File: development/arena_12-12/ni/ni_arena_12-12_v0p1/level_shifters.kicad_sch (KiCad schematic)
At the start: 15 parts, among them U1 TXB0108PW, U2 TXB0108PW, U3 TXB0108PW, U4 TXB0108PW, U5 TXB0108PW

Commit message: Worked on schematic adding series termination resistors and buffers.
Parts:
- removed C1, C10, C2, C3, C4, C5, C6, C7, C8, C9: 0.1uF, Capacitor_SMD:C_0603_1608Metric, symbol Device:C
- removed U1, U5: TXB0108PW, Package_SO:TSSOP-20_4.4x6.5mm_P0.65mm, symbol TXB0108:TXB0108PW
- added C15, C16, C17, C18, C19, C20, C21, C22, C23, C24, C25, C26, C27: 0.1uF, symbol Device:C_Small
- added R100, R101, R102, R103, R104, R105, R106, R107, R108, R109, R110, R111, R112, R113, R114, R115, R116, R117, R118, R119, R120, R121, R122, R123, R124, R125, R126, R127, R128, R129, R130, R131, R132, R133, R134, R135, R136, R137, R138, R139, R140, R141, R142, R143, R144, R145, R146, R147, R148, R149, R150, R151, R152, R153, R154, R155, R156, R157, R158, R159, R160, R41, R42, R43, R44, R45, R46, R47, R48, R49, R50, R51, R52, R53, R54, R55, R56, R57, R58, R59, R60, R61, R62, R63, R64, R65, R66, R67, R68, R69, R70, R71, R72, R73, R74, R75, R76, R77, R78, R79, R80, R81, R82, R83, R84, R85, R86, R87, R88, R89, R90, R91, R92, R93, R94, R95, R96, R97, R98, R99: 33, symbol Device:R
- added U10, U11, U12, U14, U15, U16, U18, U21, U25, U6, U7, U8: TXB0108PW, symbol TXB0108:TXB0108PW
- added U13, U17, U19, U20, U22, U23, U24, U26, U27, U28, U29, U5, U9: 74LVC2G17, symbol 74xGxx:74LVC2G17
- U2, U3, U4: footprint Package_SO:TSSOP-20_4.4x6.5mm_P0.65mm -> (none)
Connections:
- net PAN3V.SCK_01 is gone; now on an unnamed net: U2.3 (A2)
- net PAN3V.SCK_02 is gone; now on an unnamed net: U2.4 (A3)
- net PAN3V.SCK_03 is gone; now on an unnamed net: U2.5 (A4)
- net PAN3V.SCK_04 is gone; now on an unnamed net: U2.6 (A5)
- net PAN3V.SCK_05 is gone; now on an unnamed net: U2.7 (A6)
- net +3.3V: now also C15.1, C16.1, C17.1, C18.1, C19.1, C20.1, C21.1, C22.1, C23.1, C24.1, C25.1, C26.1, C27.1, U10.10 (OE), U10.2 (VCCA), U11.10 (OE), U11.2 (VCCA), U12.10 (OE), U12.2 (VCCA), U13.5 (VCC), U14.10 (OE), U14.2 (VCCA), U15.10 (OE), U15.2 (VCCA), U16.10 (OE), U16.2 (VCCA), U17.5 (VCC), U18.10 (OE), U18.2 (VCCA), U19.5 (VCC), U20.5 (VCC), U21.10 (OE), U21.2 (VCCA), U22.5 (VCC), U23.5 (VCC), U24.5 (VCC), U25.10 (OE), U25.2 (VCCA), U26.5 (VCC), U27.5 (VCC), U28.5 (VCC), U29.5 (VCC), U5.5 (VCC), U6.10 (OE), U6.2 (VCCA), U7.10 (OE), U7.2 (VCCA), U8.10 (OE), U8.2 (VCCA), U9.5 (VCC)
- net +5V: now also U10.19 (VCCB), U11.19 (VCCB), U12.19 (VCCB), U14.19 (VCCB), U15.19 (VCCB), U16.19 (VCCB), U18.19 (VCCB), U21.19 (VCCB), U25.19 (VCCB), U6.19 (VCCB), U7.19 (VCCB), U8.19 (VCCB)
- net GND: now also C15.2, C16.2, C17.2, C18.2, C19.2, C20.2, C21.2, C22.2, C23.2, C24.2, C25.2, C26.2, C27.2, U10.11 (GND), U11.11 (GND), U12.11 (GND), U13.2 (GND), U14.11 (GND), U15.11 (GND), U16.11 (GND), U17.2 (GND), U18.11 (GND), U19.2 (GND), U20.2 (GND), U21.11 (GND), U22.2 (GND), U23.2 (GND), U24.2 (GND), U25.11 (GND), U26.2 (GND), U27.2 (GND), U28.2 (GND), U29.2 (GND), U5.2 (GND), U6.11 (GND), U7.11 (GND), U8.11 (GND), U9.2 (GND)
- net PAN3V.MISO_00: now also U23.3; no longer U2.9 (A8)
- net PAN3V.MISO_01: now also U24.3; no longer U3.3 (A2)
- net PAN3V.MISO_02: now also U26.3; no longer U3.5 (A4)
- net PAN3V.MISO_03: now also U27.3; no longer U3.7 (A6)
- net PAN3V.MISO_04: now also U28.3; no longer U3.9 (A8)
- net PAN3V.MISO_05: now also U29.3; no longer U4.3 (A2)
- net PAN3V.MISO_06: no longer U4.5 (A4)
- net PAN3V.MISO_07: no longer U4.7 (A6)
- net PAN3V.MISO_08: no longer U4.9 (A8)
- net PAN3V.MOSI_00: now also U23.1; no longer U2.8 (A7)
- net PAN3V.MOSI_01: now also U24.1; no longer U3.1 (A1)
- net PAN3V.MOSI_02: now also U26.1; no longer U3.4 (A3)
- net PAN3V.MOSI_03: now also U27.1; no longer U3.6 (A5)
- net PAN3V.MOSI_04: now also U28.1; no longer U3.8 (A7)
- net PAN3V.MOSI_05: now also U29.1; no longer U4.1 (A1)
- net PAN3V.MOSI_06: no longer U4.4 (A3)
- net PAN3V.MOSI_07: no longer U4.6 (A5)
- net PAN3V.MOSI_08: no longer U4.8 (A7)
- net PAN5V.MISO_00: now also R150.1; no longer U2.12 (B8)
- net PAN5V.MISO_01: now also R152.1; no longer U3.18 (B2)
- net PAN5V.MISO_02: now also R154.1; no longer U3.16 (B4)
- net PAN5V.MISO_03: now also R156.1; no longer U3.14 (B6)
- net PAN5V.MISO_04: now also R158.1; no longer U3.12 (B8)
- net PAN5V.MISO_05: now also R160.1; no longer U4.18 (B2)
- net PAN5V.MISO_06: no longer U4.16 (B4)
- net PAN5V.MISO_07: no longer U4.14 (B6)
- net PAN5V.MISO_08: no longer U4.12 (B8)
- net PAN5V.MOSI_00: now also R149.1; no longer U2.13 (B7)
- net PAN5V.MOSI_01: now also R151.1; no longer U3.20 (B1)
- net PAN5V.MOSI_02: now also R153.1; no longer U3.17 (B3)
- net PAN5V.MOSI_03: now also R155.1; no longer U3.15 (B5)
- net PAN5V.MOSI_04: now also R157.1; no longer U3.13 (B7)
- net PAN5V.MOSI_05: now also R159.1; no longer U4.20 (B1)
- net PAN5V.MOSI_06: no longer U4.17 (B3)
- net PAN5V.MOSI_07: no longer U4.15 (B5)
- net PAN5V.MOSI_08: no longer U4.13 (B7)
- net PAN5V.SCK_00: no longer U2.20 (B1)
- net PAN5V.SCK_01: no longer U2.18 (B2)
- net PAN5V.SCK_02: no longer U2.17 (B3)
- net PAN5V.SCK_03: no longer U2.16 (B4)
- net PAN5V.SCK_04: no longer U2.15 (B5)
- net PAN5V.SCK_05: no longer U2.14 (B6)
- net PAN3V.SCK_00: no longer names the net of U2.1 (A1)
- net PAN3V.SCK_00: now also U2.8 (A7), U2.9 (A8), U3.1 (A1), U3.3 (A2), U3.4 (A3), U3.5 (A4), U5.6
- new net: U21.6 (A5), U23.6
- new net: U11.6 (A5), U11.7 (A6), U11.8 (A7), U11.9 (A8), U12.1 (A1), U12.3 (A2), U12.4 (A3), U12.5 (A4), U12.6 (A5), U12.7 (A6), U12.8 (A7), U12.9 (A8), U13.4
- new net: R112.2, U12.12 (B8)
- new net: R111.2, U12.13 (B7)
- new net: R110.2, U12.14 (B6)
- new net: R109.2, U12.15 (B5)
- new net: R108.2, U12.16 (B4)
- new net: R107.2, U12.17 (B3)
- new net: R106.2, U12.18 (B2)
- new net: R105.2, U12.20 (B1)
- new net: R128.2, U15.12 (B8)
- new net: R50.2, U3.18 (B2)
- new net: R103.2, U11.13 (B7)
- new net: R153.2, U25.20 (B1)
- new net: R82.2, U8.18 (B2)
- new net: U6.1 (A1), U6.3 (A2), U6.4 (A3), U6.5 (A4), U6.6 (A5), U6.7 (A6), U6.8 (A7), U6.9 (A8), U7.1 (A1), U7.3 (A2), U7.4 (A3), U7.5 (A4), U9.6
- new net: R80.2, U7.12 (B8)
- new net: R79.2, U7.13 (B7)
- new net: R78.2, U7.14 (B6)
- new net: R77.2, U7.15 (B5)
- new net: R76.2, U7.16 (B4)
- new net: R75.2, U7.17 (B3)
- new net: R74.2, U7.18 (B2)
- new net: R73.2, U7.20 (B1)
- new net: U7.6 (A5), U7.7 (A6), U7.8 (A7), U7.9 (A8), U8.1 (A1), U8.3 (A2), U8.4 (A3), U8.5 (A4), U8.6 (A5), U8.7 (A6), U8.8 (A7), U8.9 (A8), U9.4
- new net: R142.2, U18.14 (B6)
- new net: R113.2, U14.20 (B1)
- new net: R120.2, U14.12 (B8)
- new net: R145.2, U21.20 (B1)
- new net: R86.2, U8.14 (B6)
- new net: R49.2, U3.20 (B1)
- new net: R127.2, U15.13 (B7)
- new net: R62.2, U4.14 (B6)
- new net: R150.2, U21.14 (B6)
- new net: R56.2, U3.12 (B8)
- new net: R55.2, U3.13 (B7)
- new net: R54.2, U3.14 (B6)
- new net: R53.2, U3.15 (B5)
- new net: R52.2, U3.16 (B4)
- new net: R51.2, U3.17 (B3)
- new net: U3.6 (A5), U3.7 (A6), U3.8 (A7), U3.9 (A8), U4.1 (A1), U4.3 (A2), U4.4 (A3), U4.5 (A4), U4.6 (A5), U4.7 (A6), U4.8 (A7), U4.9 (A8), U5.4
- new net: U15.6 (A5), U15.7 (A6), U15.8 (A7), U15.9 (A8), U16.1 (A1), U16.3 (A2), U16.4 (A3), U16.5 (A4), U16.6 (A5), U16.7 (A6), U16.8 (A7), U16.9 (A8), U17.4
- new net: R136.2, U16.12 (B8)
- new net: R135.2, U16.13 (B7)
- new net: R134.2, U16.14 (B6)
- new net: R133.2, U16.15 (B5)
- new net: R132.2, U16.16 (B4)
- new net: R131.2, U16.17 (B3)
- new net: R130.2, U16.18 (B2)
- new net: R129.2, U16.20 (B1)
- new net: U18.4 (A3), U18.5 (A4), U19.4
- new net: U14.1 (A1), U14.3 (A2), U14.4 (A3), U14.5 (A4), U14.6 (A5), U14.7 (A6), U14.8 (A7), U14.9 (A8), U15.1 (A1), U15.3 (A2), U15.4 (A3), U15.5 (A4), U17.6
- new net: R126.2, U15.14 (B6)
- new net: R125.2, U15.15 (B5)
- new net: R124.2, U15.16 (B4)
- new net: R123.2, U15.17 (B3)
- new net: R122.2, U15.18 (B2)
- new net: R121.2, U15.20 (B1)
- new net: R160.2, U25.12 (B8)
- new net: U18.1 (A1), U18.3 (A2), U19.6
- new net: R154.2, U25.18 (B2)
- new net: R157.2, U25.15 (B5)
- new net: R69.2, U6.15 (B5)
- new net: R59.2, U4.17 (B3)
- new net: R88.2, U8.12 (B8)
- new net: R84.2, U8.16 (B4)
- new net: U18.6 (A5), U18.7 (A6), U20.6
- new net: U10.1 (A1), U10.3 (A2), U10.4 (A3), U10.5 (A4), U10.6 (A5), U10.7 (A6), U10.8 (A7), U10.9 (A8), U11.1 (A1), U11.3 (A2), U11.4 (A3), U11.5 (A4), U13.6
- new net: R87.2, U8.13 (B7)
- new net: R118.2, U14.14 (B6)
- new net: U25.3 (A2), U26.4
- new net: R68.2, U6.16 (B4)
- new net: R46.2, U2.14 (B6)
- new net: U25.1 (A1), U26.6
- new net: R144.2, U18.12 (B8)
- new net: R143.2, U18.13 (B7)
- new net: R141.2, U18.15 (B5)
- new net: R140.2, U18.16 (B4)
- new net: R139.2, U18.17 (B3)
- new net: R138.2, U18.18 (B2)
- new net: R137.2, U18.20 (B1)
- new net: U18.8 (A7), U18.9 (A8), U20.4
- new net: R85.2, U8.15 (B5)
- new net: R83.2, U8.17 (B3)
- new net: R81.2, U8.20 (B1)
- new net: R66.2, U6.18 (B2)
- new net: R147.2, U21.17 (B3)
- new net: R43.2, U2.17 (B3)
- new net: R89.2, U10.20 (B1)
- new net: R149.2, U21.15 (B5)
- new net: R91.2, U10.17 (B3)
- new net: U25.8 (A7), U29.6
- new net: R63.2, U4.13 (B7)
- new net: R104.2, U11.12 (B8)
- new net: R102.2, U11.14 (B6)
- new net: R101.2, U11.15 (B5)
- new net: R100.2, U11.16 (B4)
- new net: R99.2, U11.17 (B3)
- new net: R98.2, U11.18 (B2)
- new net: R97.2, U11.20 (B1)
- new net: R116.2, U14.16 (B4)
- new net: R72.2, U6.12 (B8)
- new net: R115.2, U14.17 (B3)
- new net: R146.2, U21.18 (B2)
- new net: U21.1 (A1), U21.3 (A2), U22.6
- new net: R156.2, U25.16 (B4)
- new net: U21.9 (A8), U24.4
- new net: R151.2, U21.13 (B7)
- new net: R159.2, U25.13 (B7)
- new net: R158.2, U25.14 (B6)
- new net: R155.2, U25.17 (B3)
- new net: U25.4 (A3), U27.6
- new net: U25.5 (A4), U27.4
- new net: U25.6 (A5), U28.6
- new net: U25.7 (A6), U28.4
- new net: U25.9 (A8), U29.4
- new net: R117.2, U14.15 (B5)
- new net: R119.2, U14.13 (B7)
- new net: R114.2, U14.18 (B2)
- new net: U21.7 (A6), U23.4
- new net: R70.2, U6.14 (B6)
- new net: R60.2, U4.16 (B4)
- new net: R96.2, U10.12 (B8)
- new net: R95.2, U10.13 (B7)
- new net: R94.2, U10.14 (B6)
- new net: R93.2, U10.15 (B5)
- new net: R92.2, U10.16 (B4)
- new net: R90.2, U10.18 (B2)
- new net: R152.2, U21.12 (B8)
- new net: U21.8 (A7), U24.6
- new net: R48.2, U2.12 (B8)
- new net: R71.2, U6.13 (B7)
- new net: R58.2, U4.18 (B2)
- new net: R67.2, U6.17 (B3)
- new net: R41.2, U2.20 (B1)
- new net: U21.4 (A3), U21.5 (A4), U22.4
- new net: R44.2, U2.16 (B4)
- new net: R64.2, U4.12 (B8)
- new net: R61.2, U4.15 (B5)
- new net: R57.2, U4.20 (B1)
- new net: R42.2, U2.18 (B2)
- new net: R148.2, U21.16 (B4)
- new net: R65.2, U6.20 (B1)
- new net: R45.2, U2.15 (B5)
- new net: R47.2, U2.13 (B7)
- new net PAN3V.CS_0: U5.1
- new net PAN3V.CS_1: U5.3
- new net PAN3V.CS_2: U9.1
- new net PAN3V.CS_3: U9.3
- new net PAN3V.CS_4: U13.1
- new net PAN3V.CS_5: U13.3
- new net PAN3V.CS_6: U17.1
- new net PAN3V.CS_7: U17.3
- new net PAN3V.SCK_0: U19.1
- new net PAN3V.SCK_1: U19.3
- new net PAN3V.SCK_2: U20.1
- new net PAN3V.SCK_3: U20.3
- new net PAN3V.SCK_4: U22.1
- new net PAN3V.SCK_5: U22.3
- new net PAN5V.CS_0_P01: R41.1
- new net PAN5V.CS_0_P02: R42.1
- new net PAN5V.CS_0_P03: R43.1
- new net PAN5V.CS_0_P04: R44.1
- new net PAN5V.CS_0_P05: R45.1
- new net PAN5V.CS_0_P06: R46.1
- new net PAN5V.CS_0_P07: R47.1
- new net PAN5V.CS_0_P08: R48.1
- new net PAN5V.CS_0_P09: R49.1
- new net PAN5V.CS_0_P10: R50.1
- new net PAN5V.CS_0_P11: R51.1
- new net PAN5V.CS_0_P12: R52.1
- new net PAN5V.CS_1_P01: R53.1
- new net PAN5V.CS_1_P02: R54.1
- new net PAN5V.CS_1_P03: R55.1
- new net PAN5V.CS_1_P04: R56.1
- new net PAN5V.CS_1_P05: R57.1
- new net PAN5V.CS_1_P06: R58.1
- new net PAN5V.CS_1_P07: R59.1
- new net PAN5V.CS_1_P08: R60.1
- new net PAN5V.CS_1_P09: R61.1
- new net PAN5V.CS_1_P10: R62.1
- new net PAN5V.CS_1_P11: R63.1
- new net PAN5V.CS_1_P12: R64.1
- new net PAN5V.CS_2_P01: R65.1
- new net PAN5V.CS_2_P02: R66.1
- new net PAN5V.CS_2_P03: R67.1
- new net PAN5V.CS_2_P04: R68.1
- new net PAN5V.CS_2_P05: R69.1
- new net PAN5V.CS_2_P06: R70.1
- new net PAN5V.CS_2_P07: R71.1
- new net PAN5V.CS_2_P08: R72.1
- new net PAN5V.CS_2_P09: R73.1
- new net PAN5V.CS_2_P10: R74.1
- new net PAN5V.CS_2_P11: R75.1
- new net PAN5V.CS_2_P12: R76.1
- new net PAN5V.CS_3_P01: R77.1
- new net PAN5V.CS_3_P02: R78.1
- new net PAN5V.CS_3_P03: R79.1
- new net PAN5V.CS_3_P04: R80.1
- new net PAN5V.CS_3_P05: R81.1
- new net PAN5V.CS_3_P06: R82.1
- new net PAN5V.CS_3_P07: R83.1
- new net PAN5V.CS_3_P08: R84.1
- new net PAN5V.CS_3_P09: R85.1
- new net PAN5V.CS_3_P10: R86.1
- new net PAN5V.CS_3_P11: R87.1
- new net PAN5V.CS_3_P12: R88.1
- new net PAN5V.CS_4_P01: R89.1
- new net PAN5V.CS_4_P02: R90.1
- new net PAN5V.CS_4_P03: R91.1
- new net PAN5V.CS_4_P04: R92.1
- new net PAN5V.CS_4_P05: R93.1
- new net PAN5V.CS_4_P06: R94.1
- new net PAN5V.CS_4_P07: R95.1
- new net PAN5V.CS_4_P08: R96.1
- new net PAN5V.CS_4_P09: R97.1
- new net PAN5V.CS_4_P10: R98.1
- new net PAN5V.CS_4_P11: R99.1
- new net PAN5V.CS_4_P12: R100.1
- new net PAN5V.CS_5_P01: R101.1
- new net PAN5V.CS_5_P02: R102.1
- new net PAN5V.CS_5_P03: R103.1
- new net PAN5V.CS_5_P04: R104.1
- new net PAN5V.CS_5_P05: R105.1
- new net PAN5V.CS_5_P06: R106.1
- new net PAN5V.CS_5_P07: R107.1
- new net PAN5V.CS_5_P08: R108.1
- new net PAN5V.CS_5_P09: R109.1
- new net PAN5V.CS_5_P10: R110.1
- new net PAN5V.CS_5_P11: R111.1
- new net PAN5V.CS_5_P12: R112.1
- new net PAN5V.CS_6_P01: R113.1
- new net PAN5V.CS_6_P02: R114.1
- new net PAN5V.CS_6_P03: R115.1
- new net PAN5V.CS_6_P04: R116.1
- new net PAN5V.CS_6_P05: R117.1
- new net PAN5V.CS_6_P06: R118.1
- new net PAN5V.CS_6_P07: R119.1
- new net PAN5V.CS_6_P08: R120.1
- new net PAN5V.CS_6_P09: R121.1
- new net PAN5V.CS_6_P10: R122.1
- new net PAN5V.CS_6_P11: R123.1
- new net PAN5V.CS_6_P12: R124.1
- new net PAN5V.CS_7_P01: R125.1
- new net PAN5V.CS_7_P02: R126.1
- new net PAN5V.CS_7_P03: R127.1
- new net PAN5V.CS_7_P04: R128.1
- new net PAN5V.CS_7_P05: R129.1
- new net PAN5V.CS_7_P06: R130.1
- new net PAN5V.CS_7_P07: R131.1
- new net PAN5V.CS_7_P08: R132.1
- new net PAN5V.CS_7_P09: R133.1
- new net PAN5V.CS_7_P10: R134.1
- new net PAN5V.CS_7_P11: R135.1
- new net PAN5V.CS_7_P12: R136.1
- new net PAN5V.SCK_0_H1: R137.1
- new net PAN5V.SCK_0_H2: R138.1
- new net PAN5V.SCK_1_H1: R139.1
- new net PAN5V.SCK_1_H2: R140.1
- new net PAN5V.SCK_2_H1: R141.1
- new net PAN5V.SCK_2_H2: R142.1
- new net PAN5V.SCK_3_H1: R143.1
- new net PAN5V.SCK_3_H2: R144.1
- new net PAN5V.SCK_4_H1: R145.1
- new net PAN5V.SCK_4_H2: R146.1
- new net PAN5V.SCK_5_H1: R147.1
- new net PAN5V.SCK_5_H2: R148.1

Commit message: More work on schematic adding resistos and buffers.
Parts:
- added C28, C29, C30, C31: 0.1uF, symbol Device:C_Small
- added R161, R162, R163, R164, R165, R166, R167, R168: 33, symbol Device:R
- added U30: TXB0108PW, symbol TXB0108:TXB0108PW
- added U31, U32, U33, U34: 74LVC2G17, symbol 74xGxx:74LVC2G17
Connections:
- net PAN3V.MISO_00 is gone; now on net PAN5V.MISO_00: U23.3
- net PAN3V.MISO_01 is gone; now on net PAN5V.MISO_01: U24.3
- net PAN3V.MISO_02 is gone; now on net PAN5V.MISO_02: U26.3
- net PAN3V.MISO_03 is gone; now on net PAN5V.MISO_03: U27.3
- net PAN3V.MISO_04 is gone; now on net PAN5V.MISO_04: U28.3
- net PAN3V.MISO_05 is gone; now on net PAN5V.MISO_05: U29.3
- net PAN3V.MOSI_00 is gone; now on net PAN5V.MOSI_00: U23.1
- net PAN3V.MOSI_01 is gone; now on net PAN5V.MOSI_01: U24.1
- net PAN3V.MOSI_02 is gone; now on net PAN5V.MOSI_02: U26.1
- net PAN3V.MOSI_03 is gone; now on net PAN5V.MOSI_03: U27.1
- net PAN3V.MOSI_04 is gone; now on net PAN5V.MOSI_04: U28.1
- net PAN3V.MOSI_05 is gone; now on net PAN5V.MOSI_05: U29.1
- net +3.3V: now also C28.1, C29.1, C30.1, C31.1, U30.10 (OE), U30.2 (VCCA), U31.5 (VCC), U32.5 (VCC), U33.5 (VCC), U34.5 (VCC)
- net +5V: now also U30.19 (VCCB)
- net GND: now also C28.2, C29.2, C30.2, C31.2, U30.11 (GND), U31.2 (GND), U32.2 (GND), U33.2 (GND), U34.2 (GND)
- net PAN5V.MISO_06: now also R162.1, U31.3
- net PAN5V.MISO_07: now also R164.1, U33.3
- net PAN5V.MISO_08: now also R166.1, U32.3
- net PAN5V.MISO_09: now also R168.1, U34.3
- net PAN5V.MOSI_06: now also R161.1, U31.1
- net PAN5V.MOSI_07: now also R163.1, U33.1
- net PAN5V.MOSI_08: now also R165.1, U32.1
- net PAN5V.MOSI_09: now also R167.1, U34.1
- net PAN3V.CS_0 renamed PAN5V.CS_0
- net PAN3V.CS_1 renamed PAN5V.CS_1
- net PAN3V.CS_2 renamed PAN5V.CS_2
- net PAN3V.CS_3 renamed PAN5V.CS_3
- net PAN3V.CS_4 renamed PAN5V.CS_4
- net PAN3V.CS_5 renamed PAN5V.CS_5
- net PAN3V.CS_6 renamed PAN5V.CS_6
- net PAN3V.CS_7 renamed PAN5V.CS_7
- net PAN3V.SCK_0 renamed PAN5V.SCK_0
- net PAN3V.SCK_1 renamed PAN5V.SCK_1
- net PAN3V.SCK_2 renamed PAN5V.SCK_2
- net PAN3V.SCK_3 renamed PAN5V.SCK_3
- net PAN3V.SCK_4 renamed PAN5V.SCK_4
- net PAN3V.SCK_5 renamed PAN5V.SCK_5
- new net: R161.2, U30.20 (B1)
- new net: R163.2, U30.17 (B3)
- new net: U30.9 (A8), U34.4
- new net: U30.8 (A7), U34.6
- new net: U30.1 (A1), U31.6
- new net: R166.2, U30.14 (B6)
- new net: R168.2, U30.12 (B8)
- new net: U30.6 (A5), U32.6
- new net: U30.3 (A2), U31.4
- new net: U30.4 (A3), U33.6
- new net: U30.7 (A6), U32.4
- new net: R167.2, U30.13 (B7)
- new net: R165.2, U30.15 (B5)
- new net: R164.2, U30.16 (B4)
- new net: R162.2, U30.18 (B2)
- new net: U30.5 (A4), U33.4
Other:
- moved on the sheet: C26, C27, U28C, U29C

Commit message: Worked on adding schmitt trigger and series term. resistors to level shifter.
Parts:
- added C32, C34, C35: 0.1uF, symbol Device:C_Small
- added R169, R170, R171, R172, R173, R174: 33, symbol Device:R
- added U35: TXB0108PW, symbol TXB0108:TXB0108PW
- added U36, U37, U38: 74LVC2G17, symbol 74xGxx:74LVC2G17
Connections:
- net +3.3V: now also C32.1, C34.1, C35.1, U35.10 (OE), U35.2 (VCCA), U36.5 (VCC), U37.5 (VCC), U38.5 (VCC)
- net +5V: now also U35.19 (VCCB)
- net GND: now also C32.2, C34.2, C35.2, U35.11 (GND), U36.2 (GND), U37.2 (GND), U38.2 (GND)
- net PAN5V.EXT_INT: now also R173.1
- net PAN5V.MISO_00: now also U31.1; no longer R150.1, U23.3
- net PAN5V.MISO_01: now also U31.3; no longer R152.1, U24.3
- net PAN5V.MISO_02: now also U33.1; no longer R154.1, U26.3
- net PAN5V.MISO_03: now also U33.3; no longer R156.1, U27.3
- net PAN5V.MISO_04: now also U32.1; no longer R158.1, U28.3
- net PAN5V.MISO_05: now also U32.3; no longer R160.1, U29.3
- net PAN5V.MISO_06: now also U34.1; no longer R162.1, U31.3
- net PAN5V.MISO_07: now also U34.3; no longer R164.1, U33.3
- net PAN5V.MISO_08: now also U36.1; no longer R166.1, U32.3
- net PAN5V.MISO_09: now also U36.3; no longer R168.1, U34.3
- net PAN5V.MISO_10: now also U37.1
- net PAN5V.MISO_11: now also U37.3
- net PAN5V.MOSI_00: no longer U23.1
- net PAN5V.MOSI_01: now also R150.1; no longer R151.1, U24.1
- net PAN5V.MOSI_02: now also R151.1; no longer R153.1, U26.1
- net PAN5V.MOSI_03: now also R152.1; no longer R155.1, U27.1
- net PAN5V.MOSI_04: now also R153.1; no longer R157.1, U28.1
- net PAN5V.MOSI_05: now also R154.1; no longer R159.1, U29.1
- net PAN5V.MOSI_06: now also R155.1; no longer R161.1, U31.1
- net PAN5V.MOSI_07: now also R156.1; no longer R163.1, U33.1
- net PAN5V.MOSI_08: now also R157.1; no longer R165.1, U32.1
- net PAN5V.MOSI_09: now also R158.1; no longer R167.1, U34.1
- net PAN5V.MOSI_10: now also R159.1
- net PAN5V.MOSI_11: now also R160.1
- net PAN5V.RESET: now also R174.1
- net at U30.20 (B1): now also U31.6; no longer R161.2
- net at U30.17 (B3): now also U33.6; no longer R163.2
- net at U34.4: now also U30.12 (B8); no longer U30.9 (A8)
- net at U34.6: now also U30.13 (B7); no longer U30.8 (A7)
- net at U30.1 (A1): now also R161.1; no longer U31.6
- net at U30.14 (B6): now also U32.4; no longer R166.2
- net PAN3V.MISO_07: now reaches R168.2
- net PAN3V.MISO_07: no longer U30.12 (B8)
- net at U32.6: now also U30.15 (B5); no longer U30.6 (A5)
- net at U31.4: now also U30.18 (B2); no longer U30.3 (A2)
- net at U30.4 (A3): now also R163.1; no longer U33.6
- net at U30.7 (A6): now also R166.1; no longer U32.4
- net PAN3V.MISO_06: now reaches R167.2
- net PAN3V.MISO_06: no longer U30.13 (B7)
- net PAN3V.MISO_04: now reaches R165.2
- net PAN3V.MISO_04: no longer U30.15 (B5)
- net at U30.16 (B4): now also U33.4; no longer R164.2
- net PAN3V.MISO_01: now reaches R162.2
- net PAN3V.MISO_01: no longer U30.18 (B2)
- net at U30.5 (A4): now also R164.1; no longer U33.4
- net PAN5V.CS_0 renamed PAN3V.CS_0
- net PAN5V.CS_1 renamed PAN3V.CS_1
- net PAN5V.CS_2 renamed PAN3V.CS_2
- net PAN5V.CS_3 renamed PAN3V.CS_3
- net PAN5V.CS_4 renamed PAN3V.CS_4
- net PAN5V.CS_5 renamed PAN3V.CS_5
- net PAN5V.CS_6 renamed PAN3V.CS_6
- net PAN5V.CS_7 renamed PAN3V.CS_7
- net PAN5V.SCK_0 renamed PAN3V.SCK_0
- net PAN5V.SCK_1 renamed PAN3V.SCK_1
- net PAN5V.SCK_2 renamed PAN3V.SCK_2
- net PAN5V.SCK_3 renamed PAN3V.SCK_3
- new net: R172.2, U35.5 (A4)
- new net: U35.16 (B4), U37.4
- new net: R173.2, U35.15 (B5)
- new net: R169.2, U35.1 (A1)
- new net: R174.2, U35.14 (B6)
- new net: U35.17 (B3), U37.6
- new net: U35.18 (B2), U36.4
- new net: U35.20 (B1), U36.6
- new net: R170.2, U35.3 (A2)
- new net: R171.2, U35.4 (A3)
- new net: U35.6 (A5), U38.6
- new net: U35.7 (A6), U38.4
- new net: R168.1, U30.9 (A8)
- new net: R162.1, U30.3 (A2)
- new net: R165.1, U30.6 (A5)
- new net: R167.1, U30.8 (A7)
- new net PAN3V.EXT_INT: U38.1
- new net PAN3V.MISO_00: R161.2
- new net PAN3V.MISO_02: R163.2
- new net PAN3V.MISO_03: R164.2
- new net PAN3V.MISO_05: R166.2
- new net PAN3V.MISO_08: R169.1
- new net PAN3V.MISO_09: R170.1
- new net PAN3V.MISO_10: R171.1
- new net PAN3V.MISO_11: R172.1
- new net PAN3V.MOSI_00: U23.1
- new net PAN3V.MOSI_01: U23.3
- new net PAN3V.MOSI_02: U24.1
- new net PAN3V.MOSI_03: U24.3
- new net PAN3V.MOSI_04: U26.1
- new net PAN3V.MOSI_05: U26.3
- new net PAN3V.MOSI_06: U27.1
- new net PAN3V.MOSI_07: U27.3
- new net PAN3V.MOSI_08: U28.1
- new net PAN3V.MOSI_09: U28.3
- new net PAN3V.MOSI_10: U29.1
- new net PAN3V.MOSI_11: U29.3
- new net PAN3V.RESET: U38.3
- no-connect marks 0 -> 4
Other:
- moved on the sheet: R161, R162, R163, R164, R165, R166, R167, R168, U30, U31A, U31B, U32A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

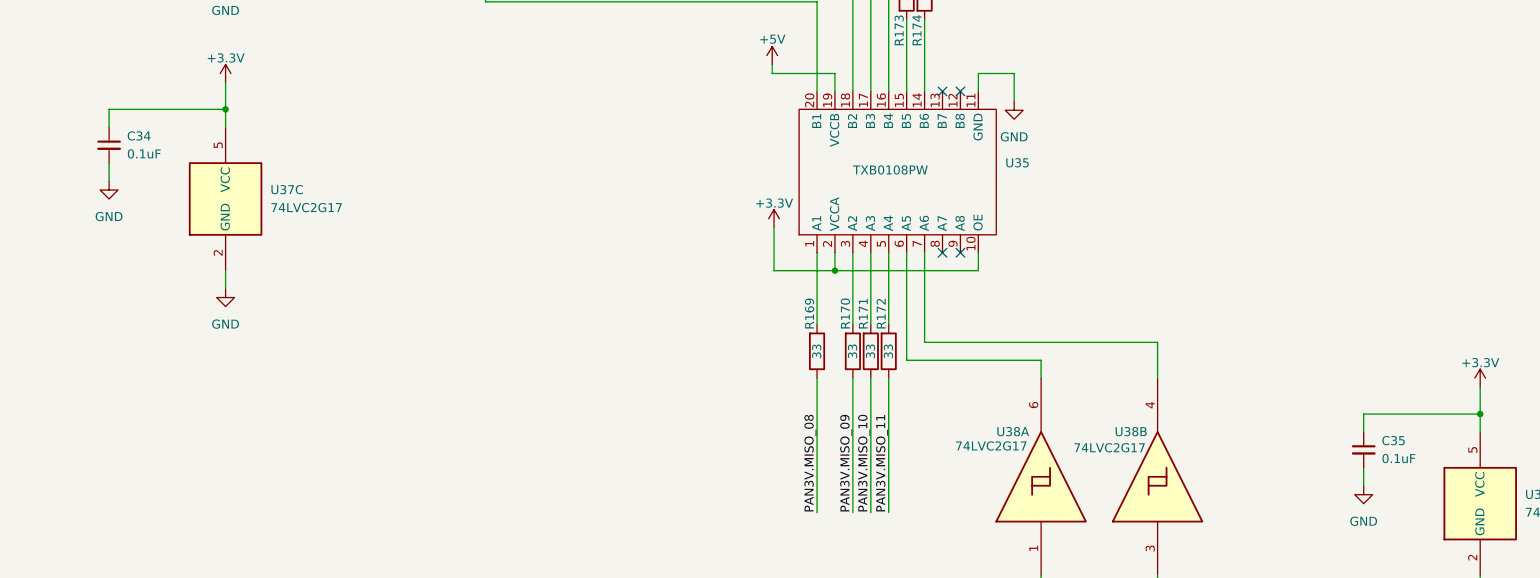
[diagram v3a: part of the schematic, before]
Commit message: Worked on 12-12 NI arena schematic.
Added schmitt trigger buffers and series termination resistors to
panels headers (not done).
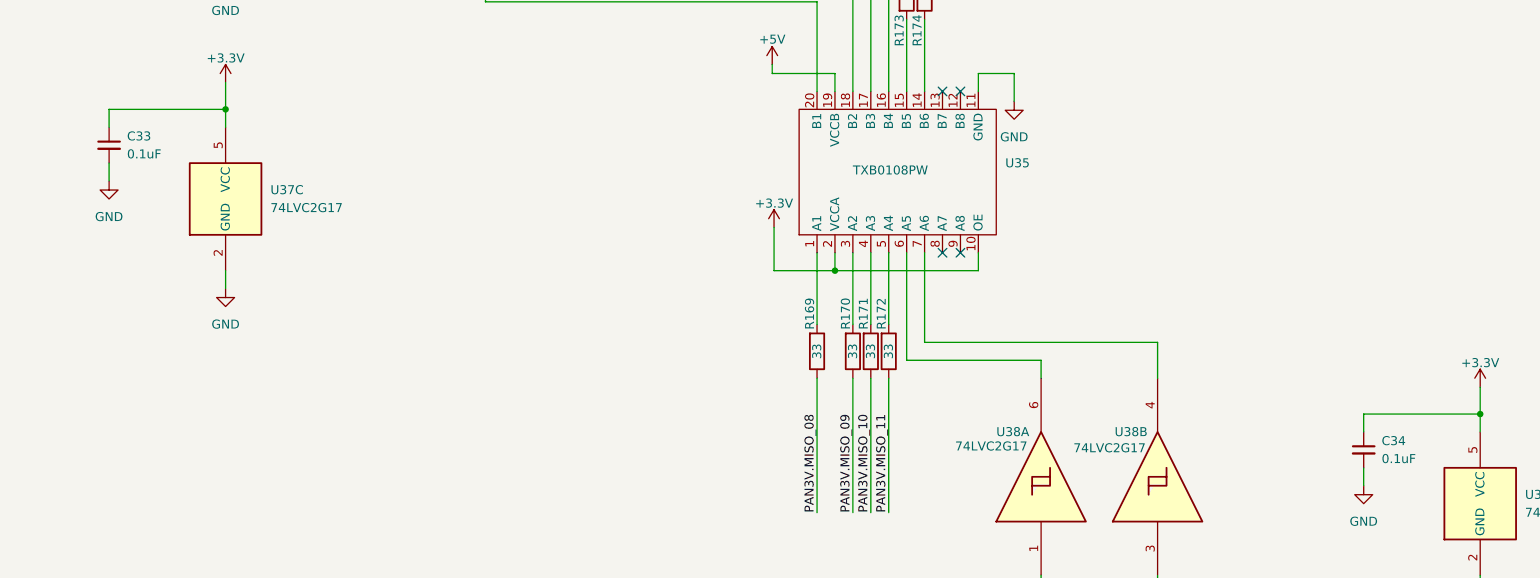
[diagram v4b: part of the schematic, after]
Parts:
- renumbered C34 to C33, C35 to C34
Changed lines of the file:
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@@
 		(dnp no)
 		(fields_autoplaced yes)
-		(property "Reference" "C34"
+		(property "Reference" "C33"
 			(at 59.69 558.8062 0)
 			(effects
@@
 			(project "ni_arena_12-12"
 				(path "/a2511654-3a17-43f1-8b9e-c45e375533dc/089bb880-f417-4f64-98ac-7a8591f9a34e"
-					(reference "C34")
+					(reference "C33")
 					(unit 1)
 				)
@@
 		(dnp no)
 		(fields_autoplaced yes)
-		(property "Reference" "C35"
+		(property "Reference" "C34"
 			(at 237.49 601.9862 0)
 			(effects
@@
 			(project "ni_arena_12-12"
 				(path "/a2511654-3a17-43f1-8b9e-c45e375533dc/089bb880-f417-4f64-98ac-7a8591f9a34e"
-					(reference "C35")
+					(reference "C34")
 					(unit 1)
 				)

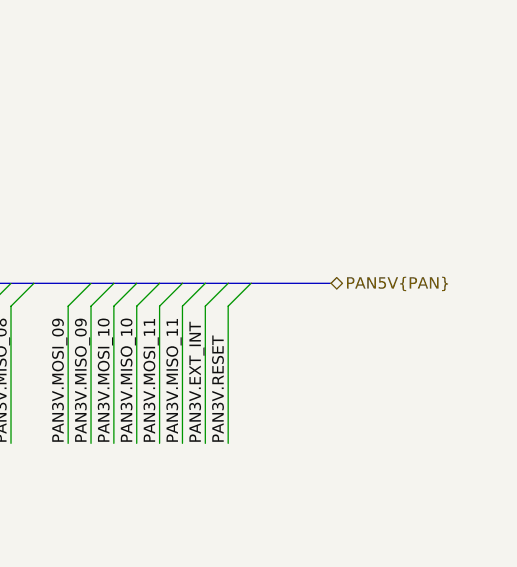
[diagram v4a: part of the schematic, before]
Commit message: Finished initial schematic for 12-12 NI with schmitt buffers.
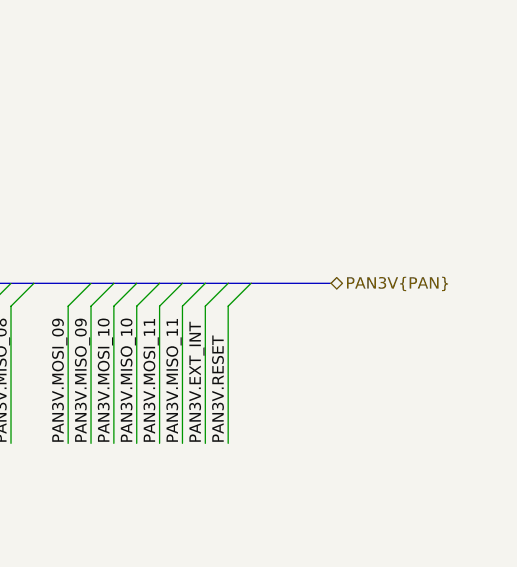
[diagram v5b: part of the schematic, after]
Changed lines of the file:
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@@
 	(generator "eeschema")
 	(generator_version "8.0")
-	(paper "User" 711.2 762)
+	(paper "User" 711.2 711.2)
 	(junction
 		(at 481.33 107.95)
@@
 		)
 	)
-	(hierarchical_label "PAN5V{PAN}"
+	(hierarchical_label "PAN3V{PAN}"
 		(shape bidirectional)
 		(at 635 582.93 0)
